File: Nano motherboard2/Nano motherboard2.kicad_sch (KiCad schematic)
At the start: 82 parts, among them IC1 RV-3028-C7, IC2 NINA-B306-00B, J1 USB_B_Mini, J2 DB15_Male_HighDensity_Mountin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, J9 SD_Card, M1 Vibration_Motor_DC, Q1 Q_PMOS_GDS, Q2 Q_PMOS_SGD, Q4 Q_NPN_BCE, SW1 SW_DIP_x01, SW2 Up, SW3 Down, SW4 Power_Switch, U1 MP5016GQH-Z, U2 XPSM82810SILT, U3 UG-2864HSWEG01

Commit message: value changes
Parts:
- removed C25: C, Capacitor_SMD:C_0805_2012Metric, symbol Device:C
- removed D5: D, Diode_SMD:D_1206_3216Metric, symbol Device:D
- BZ1: footprint CMI-9605IC-0380T:CMI9605IC0380T -> (none)
- C1, C14, C16, C6: footprint Capacitor_SMD:C_0805_2012Metric -> (none)
- C2: value 4n7 1KV -> 4n7 1kV
- C26: renamed from C?; footprint Capacitor_SMD:C_0805_2012Metric -> (none)
- C4: value C -> 22uF
- C7: value C -> 4.7nF
- D1, M1: footprint Diode_SMD:D_1206_3216Metric -> (none)
- D2: footprint Package_TO_SOT_SMD:SOT-143 -> (none)
- D3, D4: renamed from D?; footprint Diode_SMD:D_1206_3216Metric -> (none)
- FB1: footprint BLM18EG101TH1D -> (none)
- IC1: footprint RV3028C732768kHz1ppmTAQC -> (none)
- IC2: footprint NINA-B306-00B:NINAB30600B -> (none)
- Q4: footprint kicad-libraries-master:SOT23-3 -> (none)
- R1, R13, R18, R19, R2, R20, R21, R22, R5, R7, R8, R9: footprint Resistor_SMD:R_0805_2012Metric -> (none)
- R12: value R -> 10k
- R15: value R -> 402k
- R16: value R -> 88k7
- R24, R4: value R -> 47; footprint Resistor_SMD:R_0805_2012Metric -> (none)
- R25, R3: value R -> 5k; footprint Resistor_SMD:R_0805_2012Metric -> (none)
- R6: renamed from R?; footprint Resistor_SMD:R_0805_2012Metric -> (none)
- SW1: value SW_DIP_x01 -> reset
- U1: footprint QFN10-1p5X2_MNP -> (none)
- U2: footprint SIL0014B-MFG -> (none)
- U3: footprint 1X30-0.7MM -> (none)
- gave numbers to parts that had none: 3
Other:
- moved on the sheet: BZ1, Q6, R24, R25

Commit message: changes rtc etc
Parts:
- removed C10: 10pF, symbol Device:C
- removed C11, C12, C13, C4: 22uF, symbol Device:C
- removed C19, C20, C21, C23, C3: 1uF, symbol Device:C
- removed C22: 2.2uF 16V, symbol Device:C
- removed C24: 10uF, symbol Device:C
- removed C5: 39pF, symbol Device:C
- removed C7: 4.7nF, symbol Device:C
- removed IC1: RV-3028-C7, symbol RV-3028-C7:RV-3028-C7
- removed J9: SD_Card, symbol Connector:SD_Card
- removed R10, R17: 100k, symbol Device:R
- removed R11: 30k, symbol Device:R
- removed R12: 10k, symbol Device:R
- removed R14: 300k, symbol Device:R
- removed R15: 402k, symbol Device:R
- removed R16: 88k7, symbol Device:R
- removed R23: 390k, symbol Device:R
- removed U1: MP5016GQH-Z, symbol 2021-12-15_10-57-58:MP5016GQH-Z
- removed U2: XPSM82810SILT, symbol 2021-12-09_15-31-56:XPSM82810SILT
- removed U3: UG-2864HSWEG01, symbol UG-2864HSWEG01:UG-2864HSWEG01
- added C? (x2): C, symbol Device:C
- added C?: 220nF, symbol Device:C
- added C? (x3): 100nF, symbol Device:C
- added C? (x2): 22uF, symbol Device:C
- added C? (x2): 10uF, symbol Device:C
- added C?: 220pF, symbol Device:C
- added D? (x3): SCM1293A-04SO, SOT95P275X110-6N, symbol SCM1293A-04SO:SCM1293A-04SO
- added D?: D, symbol Device:D
- added D?: D_Zener, symbol Device:D_Zener
- added IC?: RV-3032-C7, RV3032C7, symbol RV-3032-C7:RV-3032-C7
- added IC?: MP2565DQ-LF-Z, SON50P300X300X100-11N-D, symbol MP2565DQ-LF-Z:MP2565DQ-LF-Z
- added J?: 503182-1852, 5031821852, symbol 503182-1852:503182-1852
- added L?: L, symbol Device:L
- added R?: 124k, symbol Device:R
- added R?: 100k, symbol Device:R
- added R?: 51k, symbol Device:R
- added R?: 200k, symbol Device:R
- added R?: 40k2, symbol Device:R
- C15: value 22uF -> 100uF
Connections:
- net +3V3: now also C?.1, C?.1, C?.1, C?.1, C?.1, C?.1, C?.1, C?.2, D?.5 (VP), D?.5 (VP), D?.5 (VP), J?.4 (VDD), L?.2, R?.1
- net AIN0_A5_SCL: now also D?.1 (CH1)
- net AIN2_A0: now also D?.6 (CH4)
- net AIN3_A1: now also D?.4 (CH3)
- net AIN5_A3: now also D?.3 (CH2)
- net AIN6_A2: now also D?.1 (CH1)
- net AIN7_A4_SDA: now also D?.6 (CH4)
- net D4: now also J?.2 (CD/DAT3)
- net D9: now also D?.3 (CH2)
- net GND: now also C?.1, C?.1, C?.2, C?.2, C?.2, C?.2, C?.2, C?.2, C?.2, D?.2 (A), D?.2 (VN), D?.2 (VN), D?.2 (VN), IC?.11 (GND_2), IC?.6 (GND_1), J?.6 (VSS), R?.1, R?.1, R?.1
- net MISO: now also J?.7 (DAT0)
- net MISO~{}: now also D?.3 (CH2)
- net MOSI: now also D?.4 (CH3), J?.3 (CMD)
- net Rx: now also D?.6 (CH4)
- net SCK: now also D?.1 (CH1), J?.5 (CLK)
- net SCL1: now also IC?.8 (SCL)
- net SDA1: now also IC?.2 (SDA)
- net Switch_volt: now also C?.2, D?.1 (K), IC?.8 (VIN_1), IC?.9 (VIN_2), R?.2; no longer C8.2, FB1.1, J1.1 (VBUS)
- net Tx: now also D?.4 (CH3)
- new net: C8.2, D?.2 (A), FB1.1, J1.1 (VBUS)
- new net: IC?.5 (FB), R?.2, R?.2
- new net: IC?.3 (EN), R?.1
- new net: C?.1, R?.2
- new net: C?.1, IC?.10 (BST)
- new net: C?.2, D?.1 (K), IC?.1 (SW_1), IC?.2 (SW_2), L?.1
- new net: IC?.7 (FREQ), R?.2
- new net: C?.2, IC?.4 (COMP)
- no-connect marks 23 -> 9
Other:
- note added: "Mosfet for SD power?"
- note removed: "Debounce caps or interupt debounce"
- note removed: "Decoupling capacitors"
- note removed: "ESD protection"
- note removed: "Mosfet for SD power? Decoupling caps"
- note removed: "Mosfet for screen power?"
- moved on the sheet: BZ1, C1, D1, J2, M1, Q5, Q6, R24, R25, R3, R4

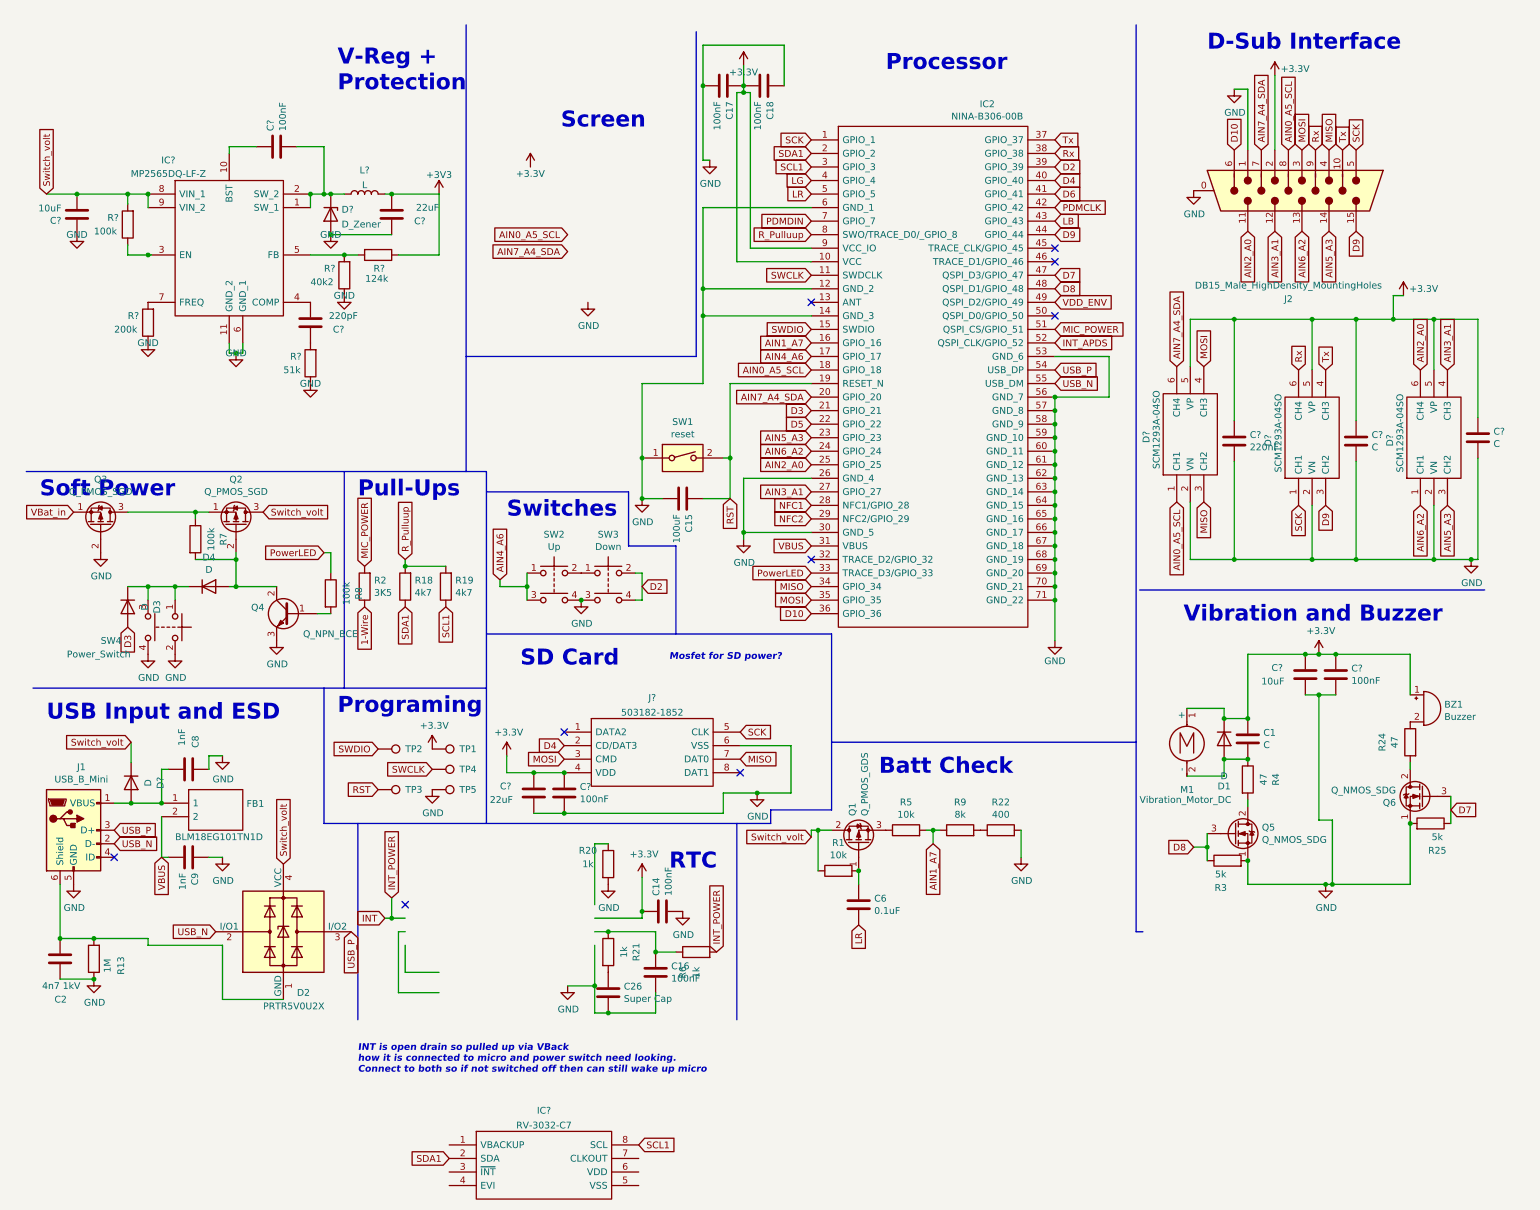
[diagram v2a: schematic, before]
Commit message: More RTC and Screen changes
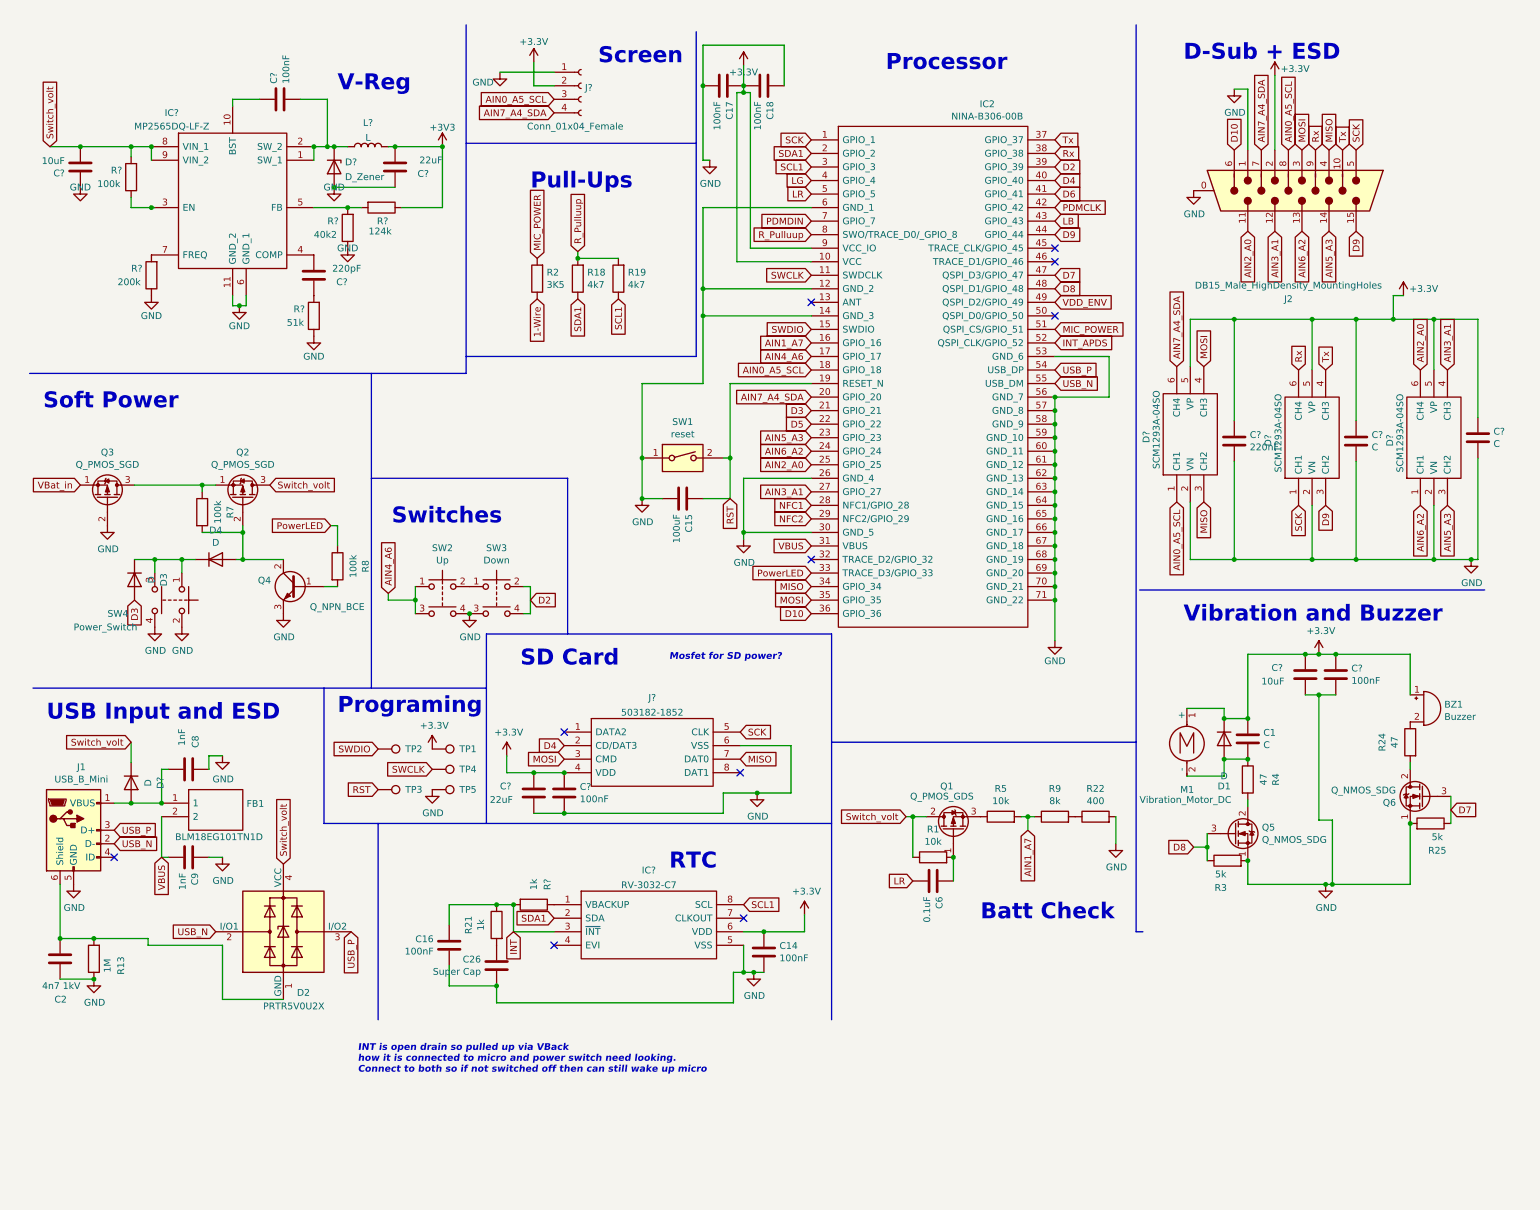
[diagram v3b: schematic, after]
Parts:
- removed R20, R6: 1k, symbol Device:R
- added J?: Conn_01x04_Female, symbol Connector:Conn_01x04_Female
- added R?: 1k, symbol Device:R
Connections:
- net +3V3: now also IC?.6 (VDD), J?.2 (Pin_2)
- net AIN0_A5_SCL: now also J?.3 (Pin_3)
- net AIN7_A4_SDA: now also J?.4 (Pin_4)
- net GND: now also IC?.5 (VSS), J?.1 (Pin_1)
- net INT: now also C16.1, IC?.3 (~{INT}), R21.1, R?.2
- net at IC?.1 (VBACKUP): now also R?.1
- no-connect marks 9 -> 10
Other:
- note added: "D-Sub + ESD"
- note added: "V-Reg"
- note removed: "D-Sub Interface"
- note removed: "V-Reg + Protection"
- moved on the sheet: C14, C16, C26, C6, C?, D3, D4, D?, IC?, L?, Q1, Q2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

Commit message: new
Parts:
- C1: value C -> 100nF
- C20, C21: renamed from C?; value C -> 220nF
- D2: footprint (none) -> DSP_PRTR5V:PRTR5V0U2X
- D7, D8, D9: renamed from D?; footprint SOT95P275X110-6N -> DSP_SCM:SOT95P275X110-6N
- IC1: renamed from IC?; footprint SON50P300X300X100-11N-D -> (none)
- IC2: footprint (none) -> DSP_NINA:NINAB30600B
- IC3: renamed from IC?; footprint RV3032C7 -> DSP_RTC:RV3032C7
- J3: renamed from J?; footprint 5031821852 -> DSP_SD:5031821852
- SW1: footprint (none) -> detect_switch:SDS001
- gave numbers to parts that had none: 19
